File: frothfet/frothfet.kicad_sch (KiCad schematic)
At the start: 8 parts, among them U1 ESP32-S3-DEVKITC

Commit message: updates
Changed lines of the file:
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@@
-	(wire
-		(pts
-			(xy 262.89 48.26) (xy 260.35 48.26)
-		)
-		(stroke
-			(width 0)
-			(type default)
-		)
-	)
 	(wire
 		(pts
@@
 			(effects
 				(font
-					(size 1.27 1.27)
-				)
-				(justify left)
-				(hide yes)
-			)
-		)
-	)
-	(global_label "ADC1_MCLK"
-		(shape input)
-		(at 262.89 48.26 0)
-		(fields_autoplaced yes)
-		(effects
-			(font
-				(size 1.27 1.27)
-			)
-			(justify left)
-		)
-		(property "Intersheetrefs" "${INTERSHEET_REFS}"
-			(at 276.7004 48.26 0)
-			(effects
-				(font

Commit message: rev e channel changes.
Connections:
- no-connect marks 16 -> 18
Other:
- sheet CHANNEL 1 ports: added LED_DIN, LED_DOUT; removed none
- sheet CHANNEL 2 ports: added LED_DIN, LED_DOUT; removed none
- sheet CHANNEL 3 ports: added LED_DIN, LED_DOUT; removed none
- sheet CHANNEL 4 ports: added LED_DIN, LED_DOUT; removed none
- sheet CHANNEL 5 ports: added LED_DIN, LED_DOUT; removed none
- sheet CHANNEL 6 ports: added LED_DIN, LED_DOUT; removed none
- sheet CHANNEL 7 ports: added LED_DIN, LED_DOUT; removed none
- sheet CHANNEL 8 ports: added LED_DIN, LED_DOUT; removed none

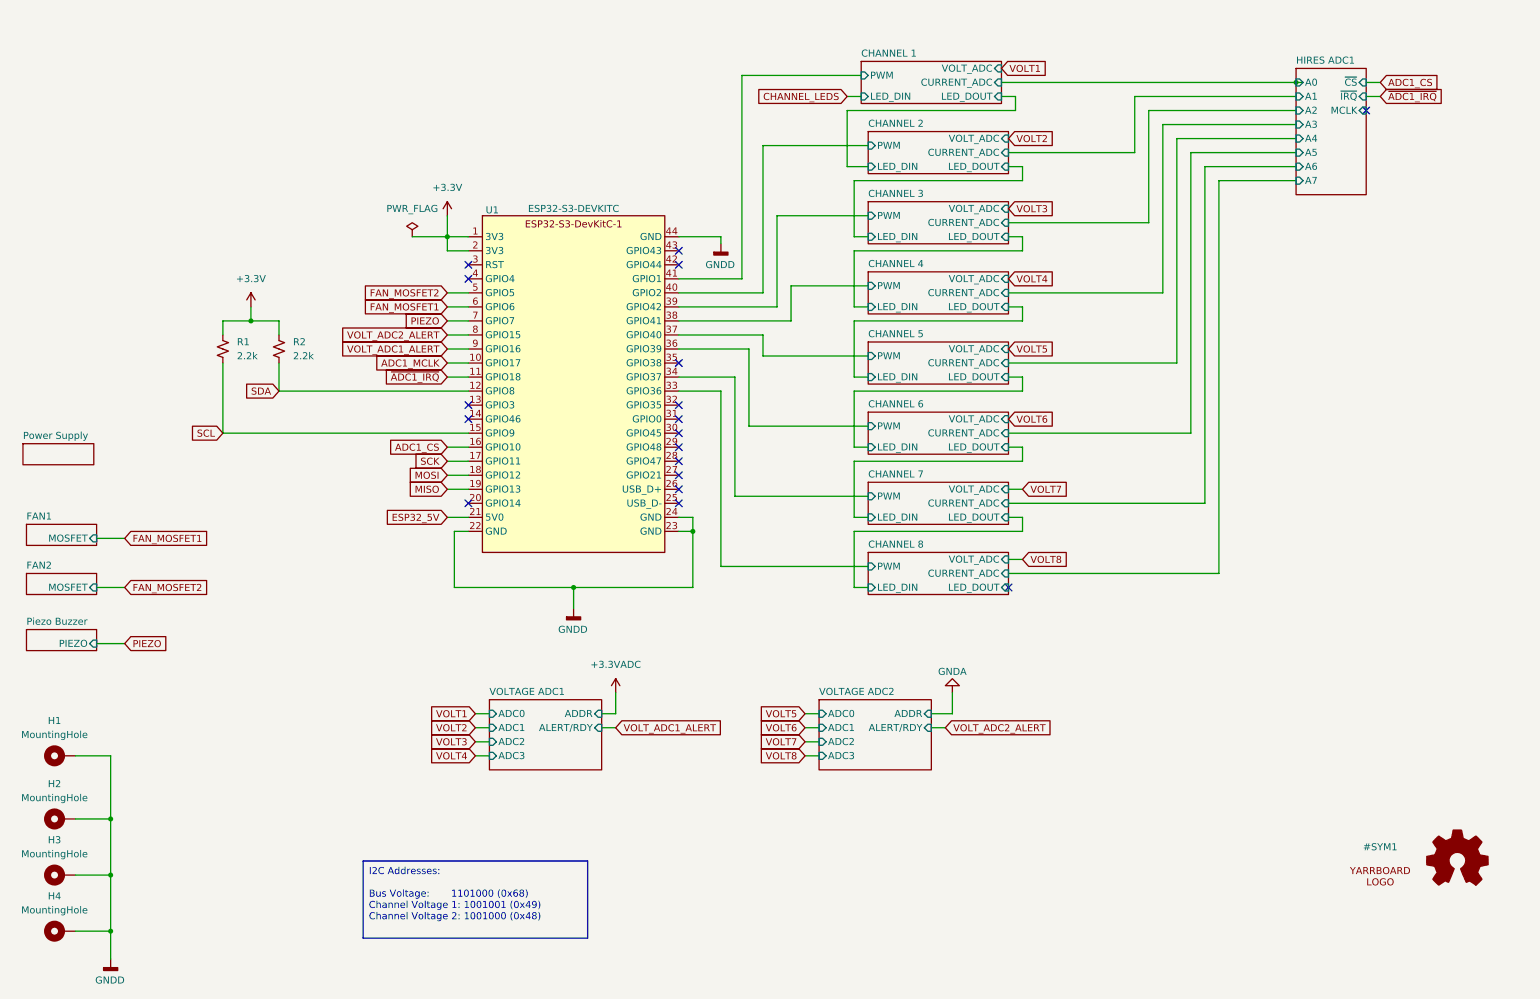
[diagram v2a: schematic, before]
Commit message: consolidated on a single adc
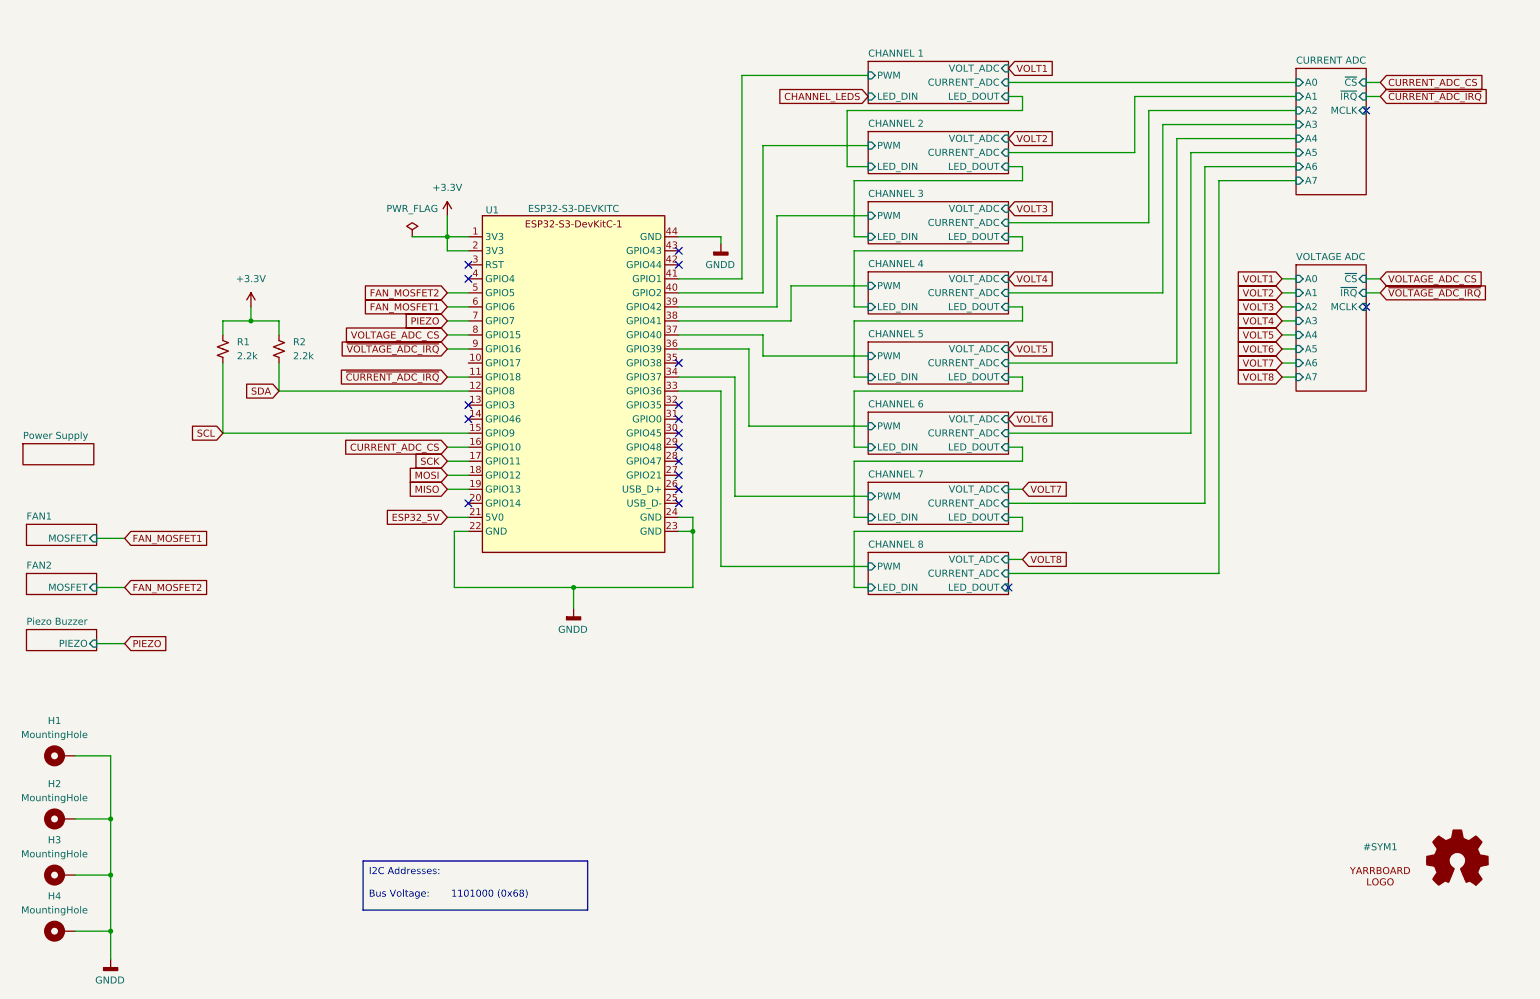
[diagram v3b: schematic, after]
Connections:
- net ADC1_CS renamed CURRENT_ADC_CS
- net ADC1_MCLK: no longer names the net of U1.10 (GPIO17)
- net VOLT_ADC1_ALERT renamed ~{VOLTAGE_ADC_IRQ}
- net VOLT_ADC2_ALERT renamed VOLTAGE_ADC_CS
- net ~{ADC1_IRQ} renamed ~{CURRENT_ADC_IRQ}
- no-connect marks 18 -> 19
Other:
- sheet HIRES ADC1 renamed CURRENT ADC
- removed sheet VOLTAGE ADC1
- removed sheet VOLTAGE ADC2
- added sheet VOLTAGE ADC (adc.kicad_sch)

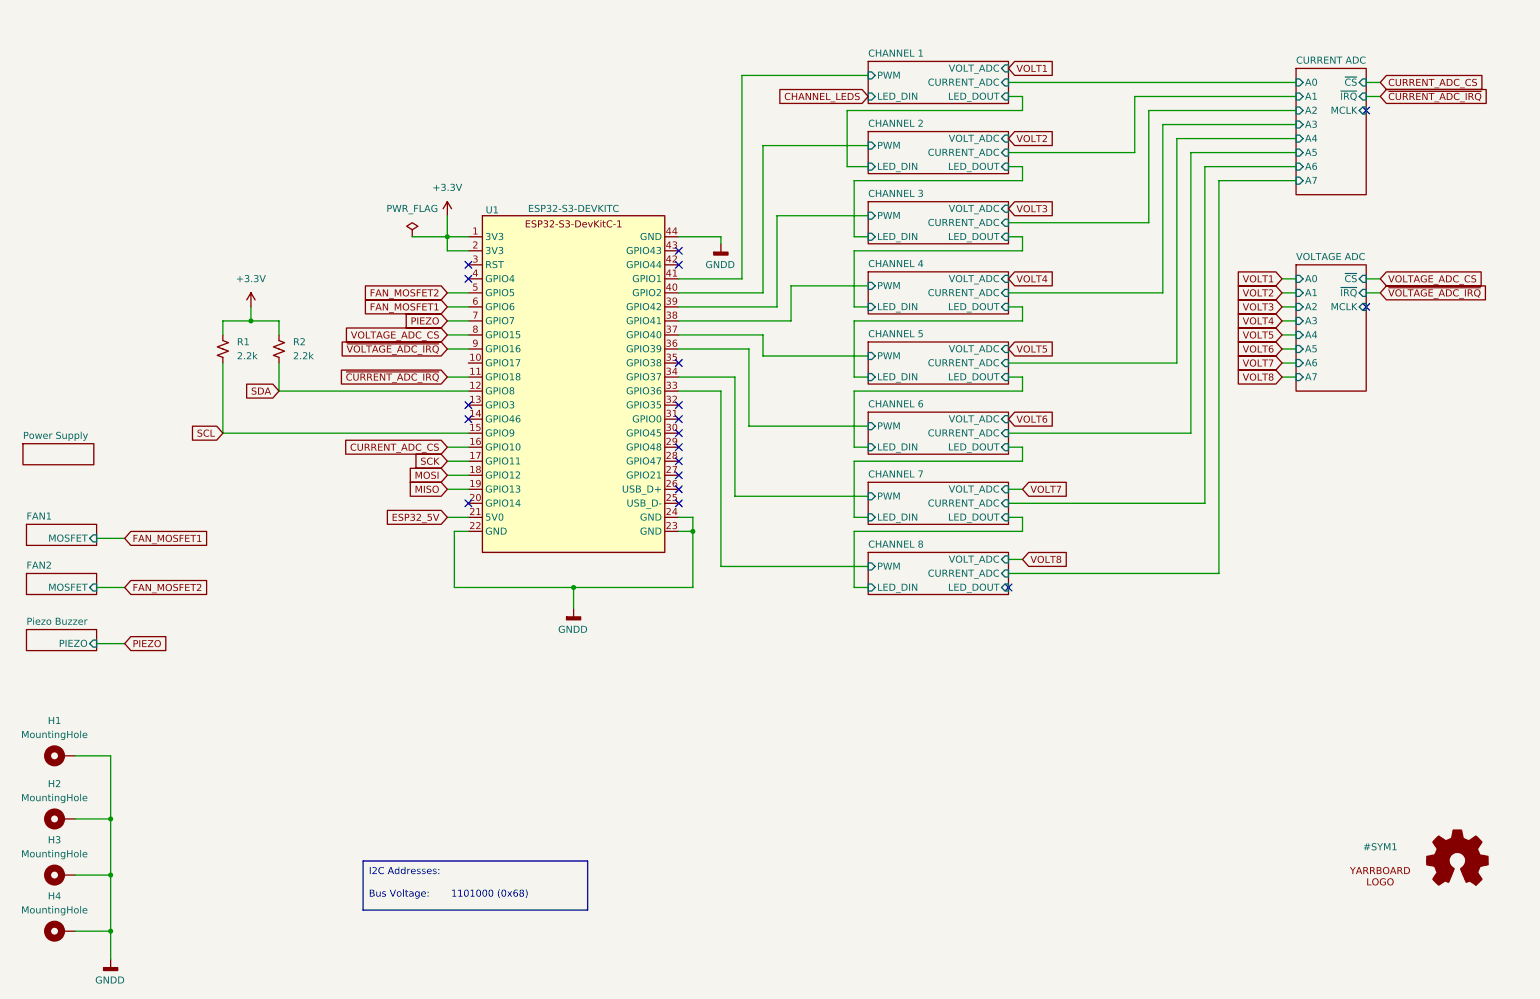
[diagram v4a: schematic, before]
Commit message: updated pins: channel rgbs + channel 5+6 pwm pins
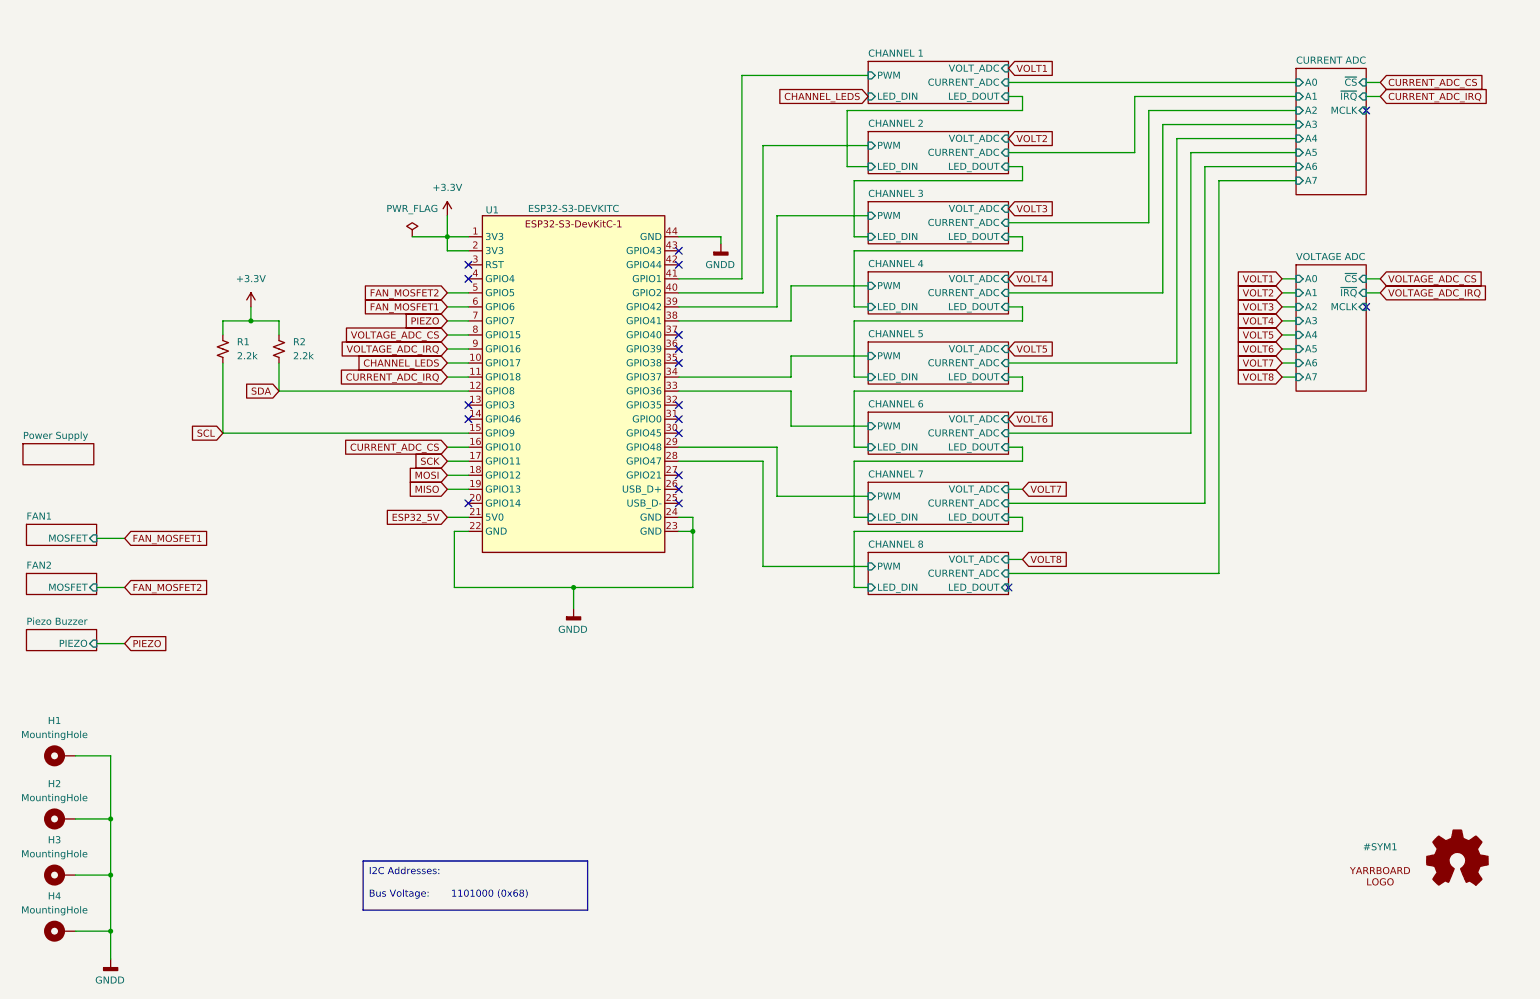
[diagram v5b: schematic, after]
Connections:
- net CHANNEL 5/PWM: now also U1.34 (GPIO37); no longer U1.37 (GPIO40)
- net CHANNEL 6/PWM: now also U1.33 (GPIO36); no longer U1.36 (GPIO39)
- net CHANNEL 7/PWM: now also U1.29 (GPIO48); no longer U1.34 (GPIO37)
- net CHANNEL 8/PWM: now also U1.28 (GPIO47); no longer U1.33 (GPIO36)
- net CHANNEL_LEDS: now also U1.10 (GPIO17)
- net ~{CURRENT_ADC_IRQ} renamed CURRENT_ADC_IRQ
- net ~{VOLTAGE_ADC_IRQ} renamed VOLTAGE_ADC_IRQ
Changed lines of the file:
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@@
+	)
+	(no_connect
+		(at 134.62 81.28)
 	)
 	(no_connect
@@
 	)
 	(no_connect
-		(at 134.62 101.6)
-	)
-	(no_connect
 		(at 134.62 109.22)
 	)
@@
 	)
 	(no_connect
-		(at 134.62 99.06)
-	)
-	(no_connect
 		(at 134.62 91.44)
 	)
@@
 	)
 	(no_connect
+		(at 134.62 78.74)
+	)
+	(no_connect
 		(at 96.52 68.58)
 	)
@@
 	(wire
 		(pts
+			(xy 154.94 88.9) (xy 134.62 88.9)
+		)
+		(stroke
+			(width 0)
+			(type default)
+		)
+	)
+	(wire
+		(pts
 			(xy 243.84 68.58) (xy 246.38 68.58)
 		)
@@
 	(wire
 		(pts
-			(xy 144.78 107.95) (xy 144.78 86.36)
+			(xy 152.4 107.95) (xy 152.4 99.06)
 		)
 		(stroke
@@
 	(wire
 		(pts
+			(xy 92.71 83.82) (xy 96.52 83.82)
+		)
+		(stroke
+			(width 0)
+			(type default)
+		)
+	)
+	(wire
+		(pts
 			(xy 25.4 154.94) (xy 31.75 154.94)
 		)
@@
 	(wire
 		(pts
-			(xy 142.24 120.65) (xy 168.91 120.65)
+			(xy 149.86 120.65) (xy 168.91 120.65)
 		)
 		(stroke
@@
 	(wire
 		(pts
+			(xy 154.94 95.25) (xy 154.94 88.9)
+		)
+		(stroke
+			(width 0)
+			(type default)
+		)
+	)
+	(wire
+		(pts
 			(xy 62.23 76.2) (xy 62.23 78.74)
 		)
@@
 	(wire
 		(pts
-			(xy 147.32 95.25) (xy 147.32 81.28)
-		)
-		(stroke
-			(width 0)
-			(type default)
-		)
-	)
-	(wire
-		(pts
 			(xy 31.75 166.37) (xy 31.75 176.53)
 		)
@@
 	(wire
 		(pts
+			(xy 149.86 120.65) (xy 149.86 101.6)
+		)
+		(stroke
+			(width 0)
+			(type default)
+		)
+	)
+	(wire
+		(pts
 			(xy 196.85 63.5) (xy 166.37 63.5)
 		)
@@
 	(wire
 		(pts
+			(xy 154.94 82.55) (xy 168.91 82.55)
+		)
+		(stroke
+			(width 0)
+			(type default)
+		)
+	)
+	(wire
+		(pts
 			(xy 92.71 81.28) (xy 96.52 81.28)
 		)
@@
 	(wire
 		(pts
+			(xy 154.94 86.36) (xy 134.62 86.36)
+		)
+		(stroke
+			(width 0)
+			(type default)
+		)
+	)
+	(wire
+		(pts
+			(xy 154.94 82.55) (xy 154.94 86.36)
+		)
+		(stroke
+			(width 0)
+			(type default)
+		)
+	)
+	(wire
+		(pts
 			(xy 222.25 40.64) (xy 222.25 71.12)
 		)
@@
 	(wire
 		(pts
-			(xy 149.86 78.74) (xy 134.62 78.74)
-		)
-		(stroke
-			(width 0)
-			(type default)
-		)
-	)
-	(wire
-		(pts
 			(xy 31.75 186.69) (xy 31.75 191.77)
 		)
@@
 	(wire
 		(pts
-			(xy 147.32 95.25) (xy 168.91 95.25)
+			(xy 154.94 95.25) (xy 168.91 95.25)
 		)
 		(stroke
@@
 	(wire
 		(pts
-			(xy 149.86 82.55) (xy 149.86 78.74)
-		)
-		(stroke
-			(width 0)
-			(type default)
-		)
-	)
-	(wire
-		(pts
 			(xy 166.37 86.36) (xy 168.91 86.36)
 		)
@@
 	(wire
 		(pts
-			(xy 144.78 86.36) (xy 134.62 86.36)
-		)
-		(stroke
-			(width 0)
-			(type default)
-		)
-	)
-	(wire
-		(pts
 			(xy 196.85 73.66) (xy 196.85 76.2)
 		)
@@
 	(wire
 		(pts
-			(xy 144.78 107.95) (xy 168.91 107.95)
+			(xy 152.4 107.95) (xy 168.91 107.95)
 		)
 		(stroke
@@
 	(wire
 		(pts
-			(xy 142.24 88.9) (xy 142.24 120.65)
-		)
-		(stroke
-			(width 0)
-			(type default)
-		)
-	)
-	(wire
-		(pts
 			(xy 243.84 73.66) (xy 246.38 73.66)
 		)
@@
 	(wire
 		(pts
+			(xy 134.62 99.06) (xy 152.4 99.06)
+		)
+		(stroke
+			(width 0)
+			(type default)
+		)
+	)
+	(wire
+		(pts
 			(xy 166.37 124.46) (xy 168.91 124.46)
 		)
@@
 	(wire
 		(pts
+			(xy 134.62 101.6) (xy 149.86 101.6)
+		)
+		(stroke
+			(width 0)
+			(type default)
+		)
+	)
+	(wire
+		(pts
 			(xy 92.71 106.68) (xy 96.52 106.68)
 		)
@@
 	(wire
 		(pts
-			(xy 147.32 81.28) (xy 134.62 81.28)
-		)
-		(stroke
-			(width 0)
-			(type default)
-		)
-	)
-	(wire
-		(pts
-			(xy 149.86 82.55) (xy 168.91 82.55)
-		)
-		(stroke
-			(width 0)
-			(type default)
-		)
-	)
-	(wire
-		(pts
 			(xy 196.85 101.6) (xy 166.37 101.6)
 		)
@@
 		(pts
 			(xy 217.17 35.56) (xy 217.17 45.72)
-		)
-		(stroke
-			(width 0)
-			(type default)
-		)
-	)
-	(wire
-		(pts
-			(xy 134.62 88.9) (xy 142.24 88.9)
 		)
 		(stroke
@@
 		)
 	)
-	(global_label "~{CURRENT_ADC_IRQ}"
+	(global_label "CURRENT_ADC_IRQ"
 		(shape input)
 		(at 92.71 86.36 180)
@@
 		)
 	)
-	(global_label "~{VOLTAGE_ADC_IRQ}"
+	(global_label "VOLTAGE_ADC_IRQ"
 		(shape input)
 		(at 92.71 81.28 180)
@@
 		)
 	)
-	(global_label "~{CURRENT_ADC_IRQ}"
+	(global_label "CURRENT_ADC_IRQ"
 		(shape input)
 		(at 261.62 35.56 0)
@@
 		)
 	)
+	(global_label "CHANNEL_LEDS"
+		(shape input)
+		(at 92.71 83.82 180)
+		(fields_autoplaced yes)
+		(effects
+			(font
+				(size 1.27 1.27)
+			)
+			(justify right)
+		)
+		(property "Intersheetrefs" "${INTERSHEET_REFS}"
+			(at 75.5734 83.82 0)
+			(effects
+				(font
+					(size 1.27 1.27)
+				)
+				(justify right)
+				(hide yes)
+			)
+		)
+	)
 	(global_label "FAN_MOSFET2"
 		(shape input)
@@
 		)
 	)
-	(global_label "~{VOLTAGE_ADC_IRQ}"
+	(global_label "VOLTAGE_ADC_IRQ"
 		(shape input)
 		(at 261.62 71.12 0)

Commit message: started work on rev e, looking clean at 13mm
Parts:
- added LOADS1: Screw_Terminal_01x08, yarrboard:KF78S-13.0-8P, symbol Connector:Screw_Terminal_01x08
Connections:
- new net LOAD1: LOADS1.1 (Pin_1)
- new net LOAD2: LOADS1.2 (Pin_2)
- new net LOAD3: LOADS1.3 (Pin_3)
- new net LOAD4: LOADS1.4 (Pin_4)
- new net LOAD5: LOADS1.5 (Pin_5)
- new net LOAD6: LOADS1.6 (Pin_6)
- new net LOAD7: LOADS1.7 (Pin_7)
- new net LOAD8: LOADS1.8 (Pin_8)
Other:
- sheet CHANNEL 1 ports: added LOAD_OUT; removed none
- sheet CHANNEL 2 ports: added LOAD_OUT; removed none
- sheet CHANNEL 3 ports: added LOAD_OUT; removed none
- sheet CHANNEL 4 ports: added LOAD_OUT; removed none
- sheet CHANNEL 5 ports: added LOAD_OUT; removed none
- sheet CHANNEL 6 ports: added LOAD_OUT; removed none
- sheet CHANNEL 7 ports: added LOAD_OUT; removed none
- sheet CHANNEL 8 ports: added LOAD_OUT; removed none
